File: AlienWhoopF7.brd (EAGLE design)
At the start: 29 x 29 mm, 55 parts, among them IC1 STM32F4/F7, M1 53047-0210, M2 53047-0210, M3 53047-0210, M4 53047-0210, Q1 IRLML6402, Q2 FDMA410NZ, Q3 FDMA410NZ, Q4 FDMA410NZ, Q5 FDMA410NZ, U1 TPS63001, U2 MPU-9250, Y1 8mhz

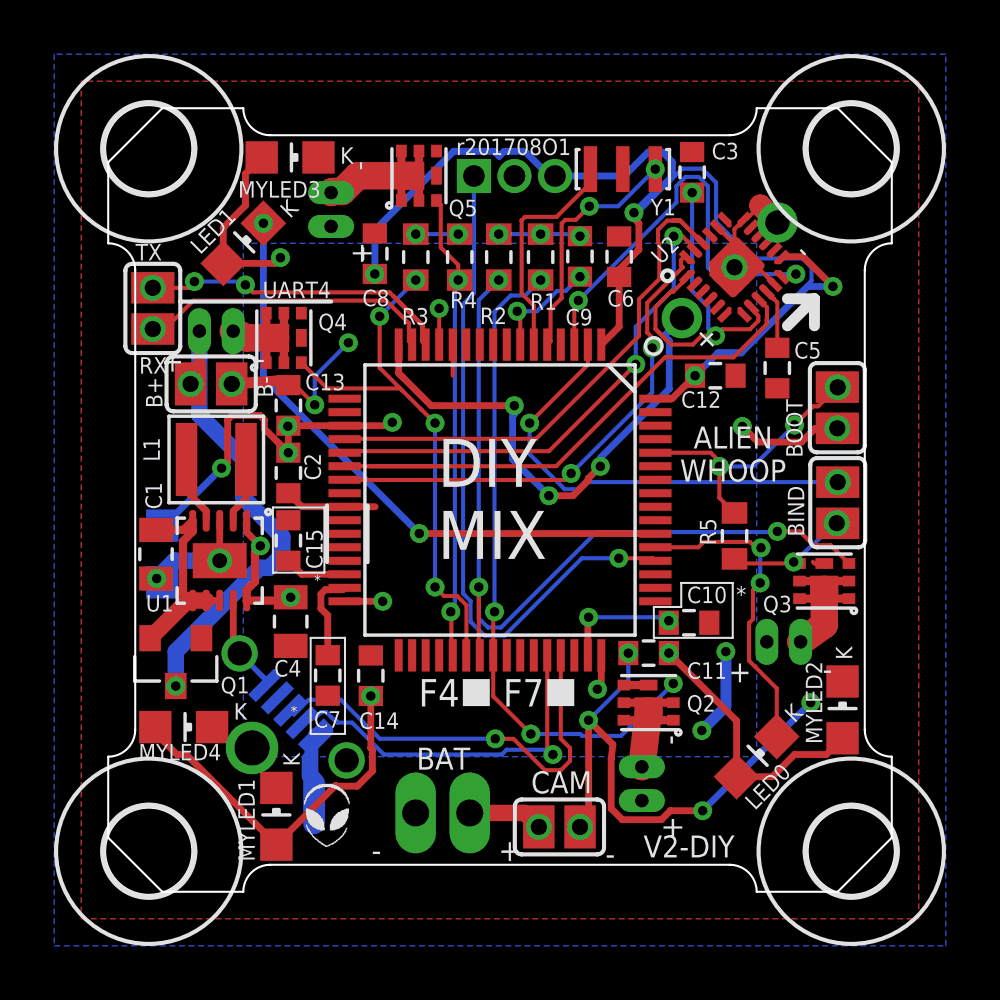
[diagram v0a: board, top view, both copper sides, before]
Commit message: Updated to V2.1 with Blackbox
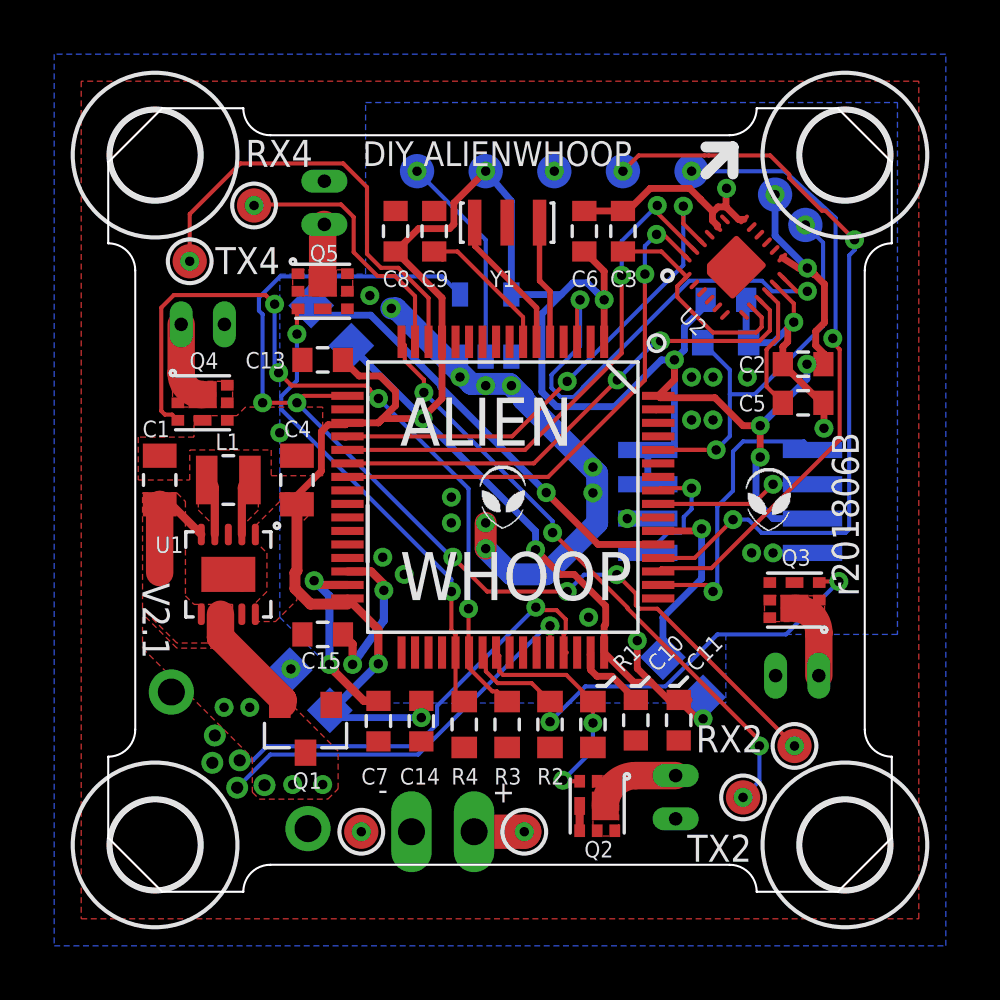
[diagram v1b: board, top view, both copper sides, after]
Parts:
- removed CAM: VTX, AlienWhoop:TINYPADS
- removed LS1: RCX03-787, AlienWhoop:RCX03-787
- removed MYLED1, MYLED2, MYLED3, MYLED4: CUSTOM, alienflight:SMD-CHIP-LED-0805
- removed PWR: BLUE, alienflight:SMD-CHIP-LED-0805
- removed RX: SBUS, alienflight:S3B-ZR
- removed SJ1: BOOT, AlienWhoop:TINYPADS
- removed SJ2: BIND, AlienWhoop:TINYPADS
- removed UART4: RXTX, AlienWhoop:TINYPADS
- removed VBAT: VBAT, AlienWhoop:TINYPADS
- added 3.3V, 3V3, BOOT, GND, GND@1, RX2, RX2/INV, RX3, RX4, TX2, TX3, TX4, VCC@1: TESTPAD, AlienWhoop:TESTPAD
- added POWER: BLUE, alienflight:SMD-CHIP-LED-0805
- added U3: MX25L6406EM2I-12G, AlienWhoop:M25P32
- added U4: SN74LVC1G04DBVR, AlienWhoop:SOT23-5
- IC1: value STM32F4/F7 -> STM32F405RGT
- L1: device alienflight:NR301X -> AlienWhoop:DFE201612E-2R2M-P2
- Q2, Q3, Q4, Q5: value FDMA410NZ -> FDMA410NZT
- U2: value MPU-9250 -> MPU-6500
- USB: value 105133-0011-SD -> 614105150621; device AlienWhoop:1051330011-SD-VIAS -> AlienWhoop:USB-BFPV
- moved LED1 22.9 mm to (21.3, 7.94), flipped to the bottom
- moved LED0 22.4 mm to (8.26, 21.0), flipped to the bottom
- moved C2 19.5 mm to (25.7, 19.5), turned to 0 degrees
- moved R3 17.6 mm to (14.8, 6.19), turned to 90 degrees
- moved R1 17.4 mm to (17.9, 6.19), turned to 90 degrees
- moved R2 17.4 mm to (16.4, 6.19), turned to 90 degrees
- moved R4 17.3 mm to (13.2, 6.19), turned to 90 degrees
- moved R5 7.16 mm to (22.9, 20.3), flipped to the bottom, turned to 180 degrees
- moved Q5 5.56 mm to (7.94, 22.2), turned to 270 degrees
- moved C9 5.48 mm to (12.1, 24.4)
- moved Q1 5.40 mm to (7.30, 6.03)
- moved C4 5.25 mm to (6.99, 15.2), turned to 90 degrees
- moved Y1 4.72 mm to (14.8, 24.8)
- moved Q2 4.27 mm to (18.1, 3.17), turned to 180 degrees
- moved C10 4.11 mm to (19.5, 6.35), turned to 90 degrees
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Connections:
- removed net BIND: IC1.2, SJ2.1
- removed net F4F7_INCOMPAT_26: IC1.26
- removed net F4F7_INCOMPAT_27: IC1.27
- removed net F4F7_INCOMPAT_28: IC1.28
- removed net F4F7_INCOMPAT_29: IC1.29
- removed net I2C1_SCL: IC1.58
- removed net I2C1_SDA: IC1.59
- removed net SPI2_MISO: IC1.35
- removed net SPI2_MOSI: IC1.36
- removed net SPI2_NSS: IC1.33
- removed net SPI2_SCK: IC1.34
- new net INV_SBUS: RX2/INV.TP, U4.2
- net 3.3V: now also 3.3V.TP, 3V3.TP, POWER.A, U3.3, U3.7, U3.8, U4.5; no longer MYLED1.A, MYLED2.A, MYLED3.A, MYLED4.A, PWR.A, RX.1, SJ1.1
- net BOOT0: now also BOOT.TP; no longer SJ1.2
- net GND: now also GND.TP, GND@1.TP, IC1.10, IC1.11, IC1.2, IC1.24, IC1.26, IC1.27, IC1.28, IC1.29, IC1.33, IC1.34, IC1.35, IC1.36, IC1.4, IC1.41, IC1.46, IC1.49, IC1.58, IC1.59, IC1.61, IC1.62, IC1.8, IC1.9, POWER.C, U3.4, U4.3, USB.P$6, USB.P$7; no longer CAM.2, LS1.-, MYLED1.C, MYLED2.C, MYLED3.C, MYLED4.C, PWR.C, RX.2, SJ2.2, U2.CENTER, USB.P$1, USB.P$2, USB.P$3, VBAT.2
- net L1: now also L1.P$1; no longer L1.1
- net L2: now also L1.P$2; no longer L1.2
- net SPI3_MISO: now also U3.2
- net SPI3_MOSI: now also U3.5
- net SPI3_NSS: now also IC1.50, U3.1; no longer IC1.4
- net SPI3_SCK: now also U3.6
- net UART2_RX: now also RX2.TP, U4.4
- net UART2_TX: now also TX2.TP; no longer LS1.+
- net UART3_RX: now also RX3.TP; no longer RX.3
- net UART3_TX: now also TX3.TP
- net UART4_RX: now also RX4.TP; no longer UART4.1
- net UART4_TX: now also TX4.TP; no longer UART4.2
- net VCC: now also VCC@1.TP; no longer CAM.1, VBAT.1
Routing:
- net UART2_RX: track 0.00 -> 39.7 mm, vias 0 -> 6
- net VCC: track 25.3 -> 1.86 mm, vias 3 -> 5
- net UART3_TX: track 0.00 -> 23.1 mm, vias 0 -> 2
- net GND: track 61.5 -> 40.7 mm, vias 20 -> 28
- net BIND: track 17.0 -> 0.00 mm, vias 2 -> 0
- net PWM1: track 24.7 -> 8.68 mm, vias 4 -> 2
- net LED1: track 22.9 -> 6.98 mm, vias 2 -> 1
- net PWM2: track 31.2 -> 17.9 mm, vias 3 -> 2
- net SPI3_NSS: track 0.00 -> 10.8 mm, vias 0 -> 1
- net PWM3: track 20.2 -> 29.1 mm
- net 3.3V: track 106.9 -> 115.2 mm, vias 18 -> 14
- net INV_SBUS: track 0.00 -> 7.92 mm, vias 0 -> 1
- net BOOT0: track 10.2 -> 17.0 mm, vias 3 -> 2
- net SPI3_MISO: track 0.00 -> 6.01 mm, vias 0 -> 1
- net VDDIO: track 13.5 -> 8.28 mm, vias 2 -> 0
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- added copper zone on layer 1, net 3.3V
- added copper zone on layer 16, net GND
- added copper zone on layer 1, net L1
- added copper zone on layer 1, net L2
- added copper zone on layer 1, net MOTOR1
- added copper zone on layer 1, net MOTOR2
- added copper zone on layer 1, net MOTOR3
- added copper zone on layer 1, net MOTOR4
- added copper zone on layer 1, net VCC
- added copper zone on layer 1, net VCC-REG
- removed copper zone on layer 16, net 3.3V
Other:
- board text added: "20180607-STEVENSON REMIX OF ALIENFLIGHT F3 LICENSE: CC BY-SA 4.0 WWW.ALIENWHOOP.US"
- board text added: "ALIEN"
- board text added: "ALIENWHOOP"
- board text added: "DIY"
- board text added: "DIY ALIENWHOOP"
- board text added: "INVER"
- board text added: "RX2"
- board text added: "Remixed from the AlienFlight F3 brushed quad by Charles Stevenson Lance's original work available at http://alienflight.com/f3-brushed-quad/"
- board text added: "USB"
- board text added: "V2.1"
- board text added: "WHOOP"
- board text added: "r201806B"
- board text removed: "*"
- board text removed: "+"
- board text removed: "-"
- board text removed: "20170807-O1-STEVENSON REMIX OF ALIENFLIGHT F3 LICENSE: CC BY-SA 4.0 WWW.ALIENWHOOP.US DIY VERSION"
- board text removed: "3.3V"
- board text removed: "ALIEN WHOOP"
- board text removed: "ALIENWHOOP DIY MIX"
- board text removed: "B+"
- board text removed: "B-"
- board text removed: "BAT"
- board text removed: "BEEP"
- board text removed: "BIND"
- board text removed: "BOOT"
- board text removed: "DIY MIX"
- board text removed: "F4"
- board text removed: "F7"
- board text removed: "GND"
- board text removed: "RX"
- board text removed: "Remixed from the AlienFlight F3 brushed quad by Charles Stevenson Lance's original design archived at http://f3-quad.alienwhoop.us/"
- board text removed: "SBUS RX"
- board text removed: "TX"
- board text removed: "UART4"
- board text removed: "V2-DIY"
- board text removed: "r201708O1"
